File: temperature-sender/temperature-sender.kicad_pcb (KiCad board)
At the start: 2 copper layers, 25 parts, among them P1 CONN_01X02, P2 CONN_01X02, P3 CONN_01X02, P4 CONN_01X02, P5 CONN_01X02, SW1 SW_PUSH, SW2 SW_PUSH, U1 MCP1700T-3302E/T, U2 ATmega32U4-AU

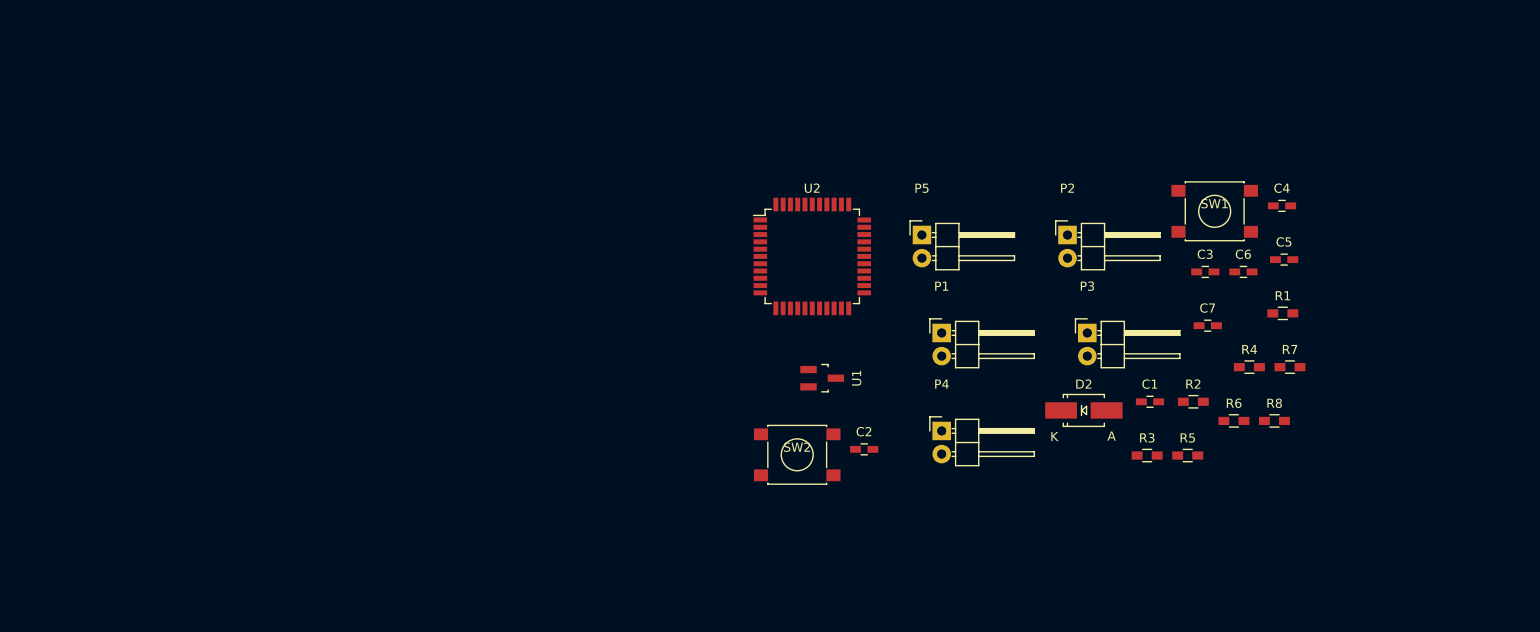
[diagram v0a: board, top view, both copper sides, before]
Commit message: More changes to temperature-sender
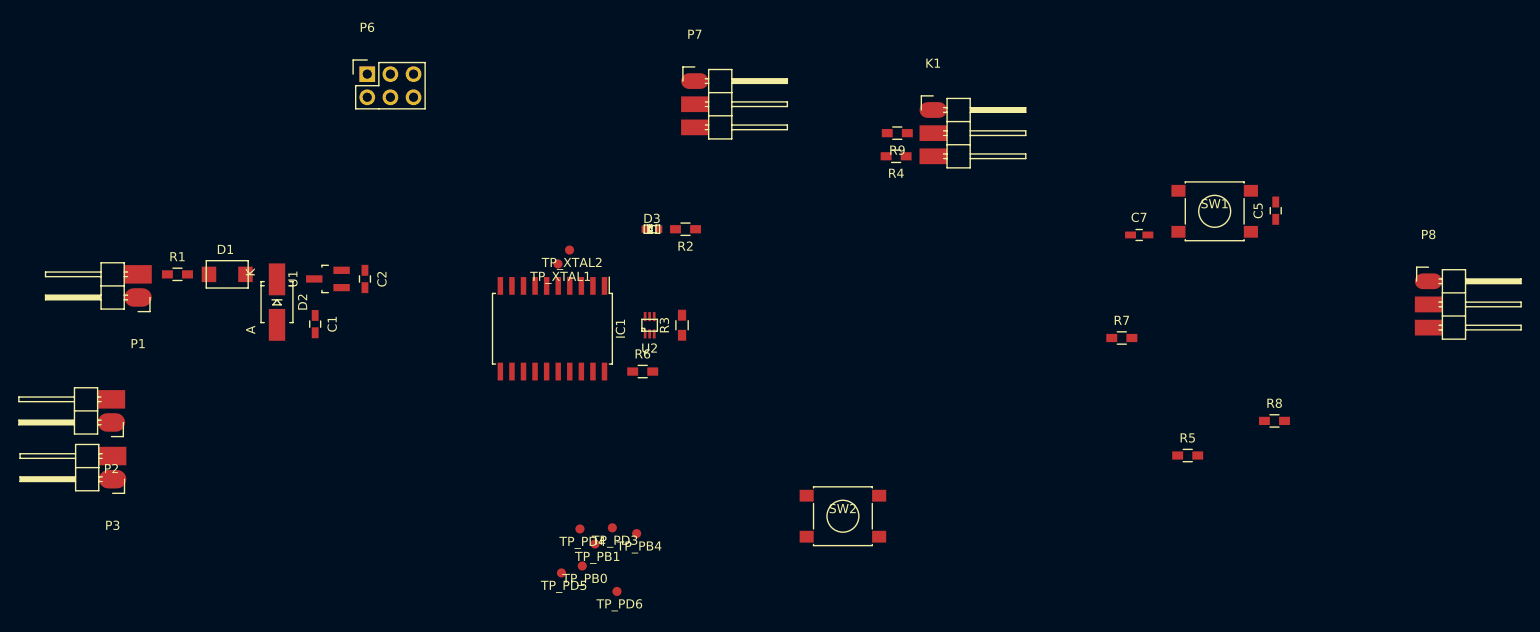
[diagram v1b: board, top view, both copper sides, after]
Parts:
- removed C3: 1uF, Capacitors_SMD:C_0603_HandSoldering
- removed C4, C6: 16pF, Capacitors_SMD:C_0603_HandSoldering
- removed P4, P5: CONN_01X02, Pin_Headers:Pin_Header_Angled_1x02
- added D1: D, kicad-footprints:DO-214AC, F.Cu at (91.3, 126.1)
- added D3: Led_Small, LEDs:LED-0603, F.Cu at (137.9, 121.2)
- added IC1: ATTINY2313A-S, Housings_SOIC:SOIC-20_7.5x12.8mm_Pitch1.27mm, F.Cu at (127.0, 132.1)
- added K1: SERVO, kicad-footprints:Pin_Header_Angled_SMD_1x03, F.Cu at (168.8, 108.1)
- added P6: ISP, Socket_Strips:Socket_Strip_Straight_2x03, F.Cu at (106.7, 104.1)
- added P7: CONN_01X03, kicad-footprints:Pin_Header_Angled_SMD_1x03, F.Cu at (142.6, 104.9)
- added P8: CONN_01X03, kicad-footprints:Pin_Header_Angled_SMD_1x03, F.Cu at (223.1, 126.9)
- added R9: 47R, Resistors_SMD:R_0603_HandSoldering, F.Cu at (164.8, 110.6)
- added TP_PB0: TEST_POINT, kicad-footprints:TP_1mm, F.Cu at (130.2, 158.1)
- added TP_PB1: TEST_POINT, kicad-footprints:TP_1mm, F.Cu at (131.6, 155.7)
- added TP_PB4: TEST_POINT, kicad-footprints:TP_1mm, F.Cu at (136.1, 154.6)
- added TP_PD3: TEST_POINT, kicad-footprints:TP_1mm, F.Cu at (133.5, 153.9)
- added TP_PD4: TEST_POINT, kicad-footprints:TP_1mm, F.Cu at (129.9, 154.1)
- added TP_PD5: TEST_POINT, kicad-footprints:TP_1mm, F.Cu at (127.9, 158.9)
- added TP_PD6: TEST_POINT, kicad-footprints:TP_1mm, F.Cu at (134.0, 160.9)
- added TP_XTAL1: TEST_POINT, kicad-footprints:TP_1mm, F.Cu at (127.5, 125.0)
- added TP_XTAL2: TEST_POINT, kicad-footprints:TP_1mm, F.Cu at (128.8, 123.4)
- C2: value C -> 1uF
- D2: value MAX 6v -> 5.1v
- P1, P2, P3: footprint Pin_Headers:Pin_Header_Angled_1x02 -> kicad-footprints:Pin_Header_Angled_SMD_1x02
- R1: value 100R -> ?R
- R3: value 22R -> 5k
- R4: value 22R -> 47R
- U1: value MCP1700T-3302E/T -> MCP1700T-3302E/TT
- U2: value ATmega32U4-AU -> TMP102; footprint Housings_QFP:TQFP-44_10x10mm_Pitch0.8mm -> kicad-footprints:SOT563
- moved R1 121.4 mm to (85.9, 126.1)
- moved P3 108.2 mm to (78.7, 148.6), turned to 180 degrees
- moved P2 106.9 mm to (78.6, 142.4), turned to 180 degrees
- moved C1 92.0 mm to (101.0, 131.6), turned to 270 degrees
- moved D2 89.3 mm to (96.8, 129.2), turned to 270 degrees
- moved P1 88.3 mm to (81.5, 128.7), turned to 180 degrees
- moved R6 65.1 mm to (136.9, 136.8)
- moved R2 58.9 mm to (141.6, 121.2), turned to 180 degrees
- moved C2 57.9 mm to (106.4, 126.6), turned to 270 degrees
- moved U1 55.3 mm to (102.4, 126.6), turned to 90 degrees
- moved R3 53.0 mm to (141.2, 131.7), turned to 90 degrees
- moved R4 45.1 mm to (164.7, 113.2), turned to 180 degrees
- moved U2 19.4 mm to (137.7, 131.7)
- moved R7 18.7 mm to (189.5, 133.1)
- moved C7 12.5 mm to (191.4, 121.8)
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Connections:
- C5 pad 1: Net-(C5-Pad1) -> /RESET
- P2 pad 1: /SDA -> /SDA/MOSI
- P3 pad 2: /+3.3v -> +3V3
- R3 pad 1: Net-(R3-Pad1) -> /ALERT
- R3 pad 2: /D+ -> +3V3
- R4 pad 1: Net-(R4-Pad1) -> Net-(K1-Pad3)
- R4 pad 2: /D- -> /SERVO1
- R5 pad 1: Net-(C5-Pad1) -> +3V3
- R5 pad 2: +3V3 -> /RESET
- R8 pad 2: /SDA -> /SDA/MOSI
- SW1 pad 2: Net-(C5-Pad1) -> /RESET
- U1 pad 1: Net-(C1-Pad1) -> GND
- U1 pad 2: GND -> +3V3
- U1 pad 3: +3V3 -> Net-(C1-Pad1)
- U2 pad 1: Net-(U2-Pad1) -> /SCL
- U2 pad 2: +3V3 -> GND
- U2 pad 3: Net-(R4-Pad1) -> /ALERT
- U2 pad 4: Net-(R3-Pad1) -> +3V3
- U2 pad 5: GND -> +3V3
- U2 pad 6: Net-(C3-Pad1) -> /SDA/MOSI
